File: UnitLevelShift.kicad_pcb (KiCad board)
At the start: 2 copper layers, 21.5 x 28.3 mm, 13 parts, among them J1 Conn_01x04_Pin, J2 Conn_01x04_Pin, Q1 2N7002, Q2 2N7002, U1 XC6206PxxxMR

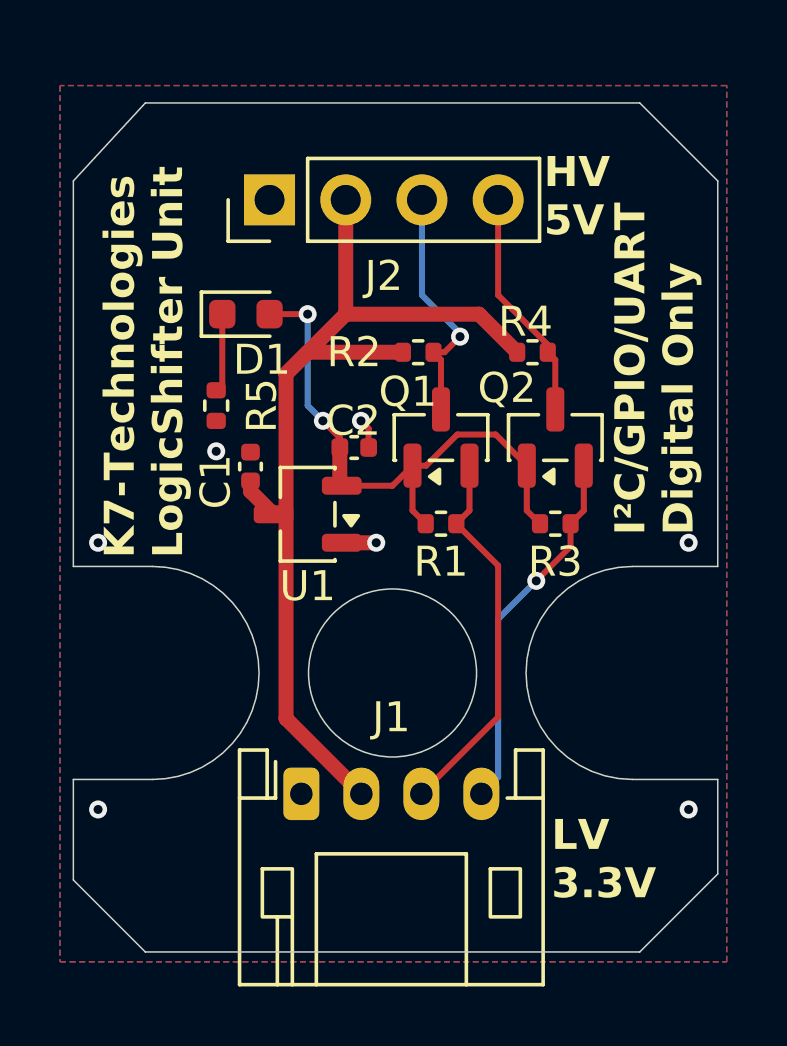
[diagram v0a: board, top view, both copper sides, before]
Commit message: Changed LED to optional mounting.
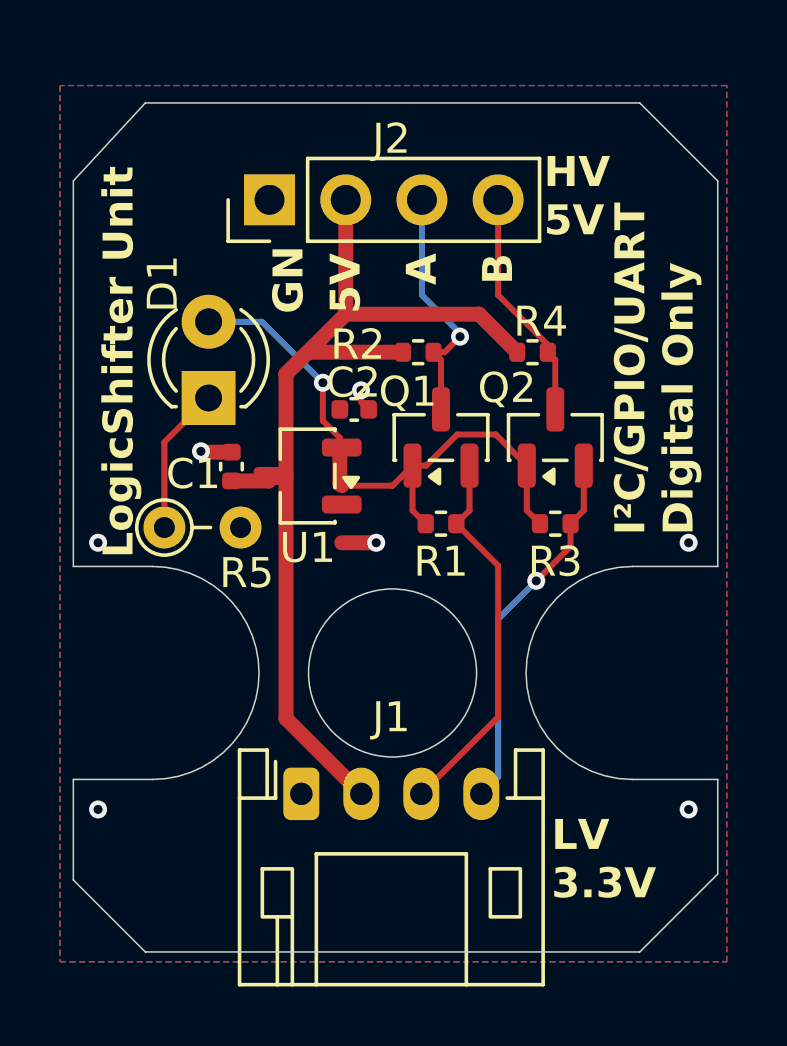
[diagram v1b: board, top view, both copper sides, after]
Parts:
- D1: footprint LED_SMD:LED_0603_1608Metric -> LED_THT:LED_D3.0mm
- R5: footprint Resistor_SMD:R_0402_1005Metric -> Resistor_THT:R_Axial_DIN0204_L3.6mm_D1.6mm_P2.54mm_Vertical
- moved R5 4.42 mm to (100.6, 85.9), turned to 0 degrees
- moved D1 3.06 mm to (102.1, 81.5), turned to 90 degrees
- moved U1 1.27 mm to (105.4, 84.1)
- moved C2 1.27 mm to (107.0, 81.9)
- moved C1 0.63 mm to (102.9, 83.8)
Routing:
- net Net-(D1-K): track 2.62 -> 5.22 mm
- net +3.3V: track 19.0 -> 19.9 mm, vias 2 -> 1
- net GND: track 2.14 -> 2.92 mm
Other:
- board text added: "5V"
- board text added: "A"
- board text added: "B"
- board text added: "GN"
- board text added: "LogicShifter Unit"
- board text removed: "K7-Technologies LogicShifter Unit"
